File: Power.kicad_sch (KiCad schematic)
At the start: 97 parts, among them Q1 FDMC510P, U1 ZXCT1009F, U2 LT1763, U3 TPS62110, U34 LT3097, U35 LT8582, U36 TPS82150

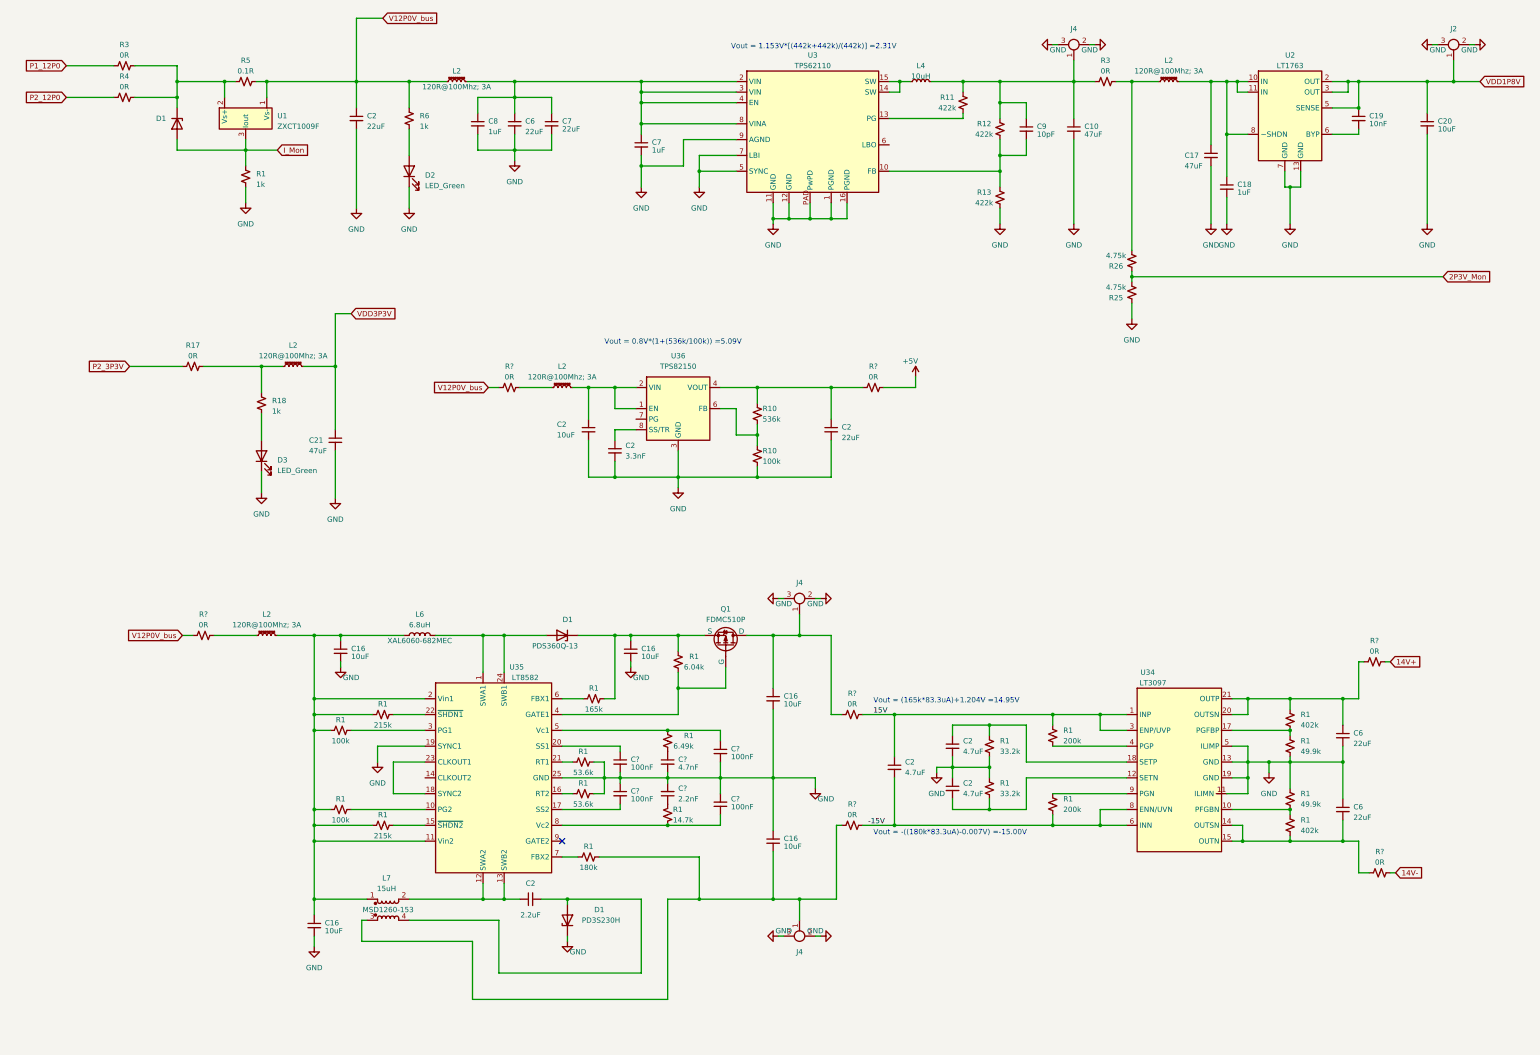
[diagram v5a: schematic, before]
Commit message: Updated Schematic
-Changed PPS input signal buffer
-Made Tweaks to Power Supply section  (Many involving the LT3097) as suggested by Trent.
- general schematic clean up for readability
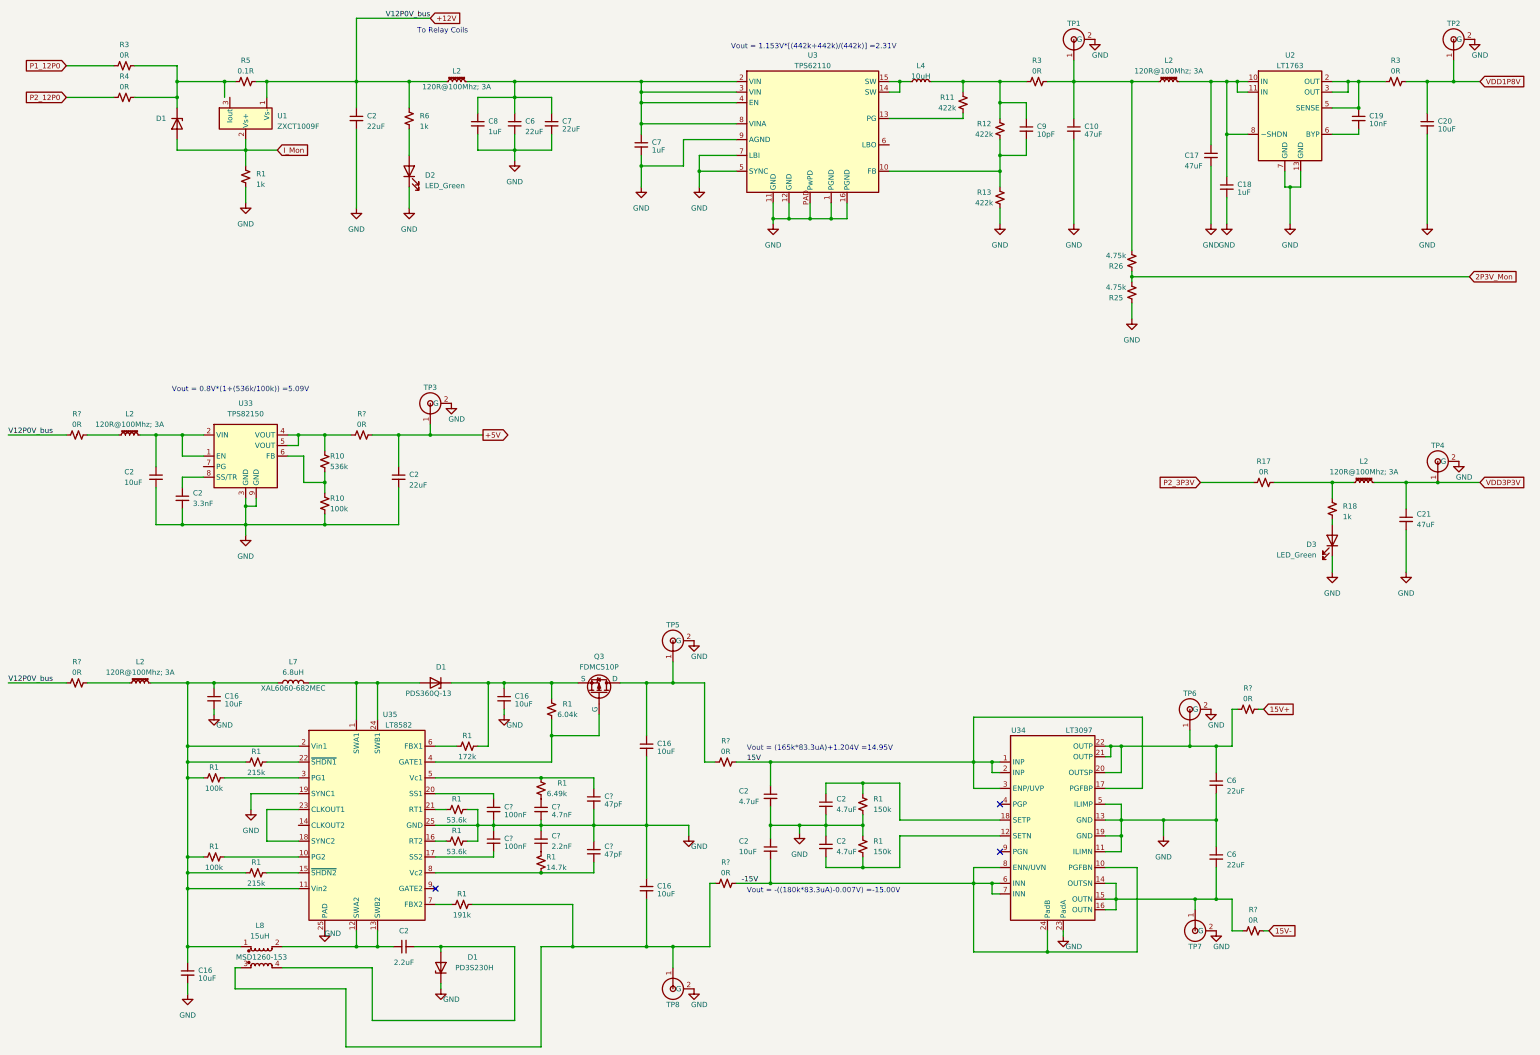
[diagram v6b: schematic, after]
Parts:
- removed J2, J4 (x3): ~, symbol Custom_Lib_MPEX_Zest:CONN_U-FL_SMD
- removed R1 (x2): 49.9k, symbol Device:R_Small_US
- removed R1: 33.2k, symbol Device:R_Small_US
- removed R1 (x2): 200k, symbol Device:R_Small_US
- removed R1 (x2): 402k, symbol Device:R_Small_US
- removed R3: 0R, symbol Device:R_Small_US
- removed R?: 0R, Capacitor_SMD:C_0603_1608Metric, symbol Device:R_Small_US
- added C2: 10uF, symbol Device:C_Small
- added R1: 150k, Resistor_SMD:R_0603_1608Metric, symbol Device:R_Small_US
- added R3 (x2): 0R, symbol Device:R_Small_US
- added R?: 0R, Capacitor_SMD:C_0603_1608Metric, symbol Device:R_Small_US
- added TP1, TP2, TP3, TP4, TP5, TP6, TP7, TP8: ~, symbol AD7768_Digitizer_SLib:Test_Point_MMCC
- C? (x2): value 100nF -> 47pF; MPN CL10B104KB8NNWC -> (none)
- R1: value 33.2k -> 150k; footprint (none) -> Resistor_SMD:R_0603_1608Metric
- R1: value 165k -> 172k
- R1: value 180k -> 191k
- renumbered L6 to L7, L7 to L8, Q1 to Q3, U36 to U33
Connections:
- net +5V: now also C2.1, R?.2, TP3.1
- net -15V: now also U34.10 (PGFBN), U34.24 (PadB), U34.7 (INN), C2.2; no longer C2.2
- net 15V: now also U34.17 (PGFBP), U34.2 (INP)
- net GND: now also C2.2, U34.23 (PadA), C2.1, R1.1, TP1.2 (G), TP2.2 (G), TP3.2 (G), TP4.2 (G), TP5.2 (G), TP6.2 (G), TP7.2 (G), TP8.2 (G)
- net I_Mon: now also U1.2 (Vs+); no longer U1.3 (Iout)
- net VDD1P8V: now also R3.2, TP2.1; no longer C19.1, U2.2 (OUT), U2.3 (OUT), U2.5 (SENSE)
- net VDD3P3V: now also TP4.1
- net at C2.2, U34.12 (SETN): now also R1.2
- net at C16.1, Q3.1 (D), R?.1: now also TP5.1
- net at C6.2, R?.1, U34.14 (OUTSN)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: now also U34.16 (OUTN), TP7.1
- net at C6.1, R?.1, U34.20 (OUTSP)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: now also U34.22 (OUTP), TP6.1
- net at C16.2, L8.3, R1.2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: now also TP8.1
- net at C9.1, L4.2, R11.1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: now also R3.1; no longer C10.1
- net at L2.1, R26.2: now also C10.1, R3.2, TP1.1
- net at R10.1, U33.4 (VOUT), U33.5 (VOUT): now also R?.1; no longer C2.1
- net at D1.1 (K), R3.2, R4.2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: no longer U1.2 (Vs+)
- net 14V+ renamed 15V+
- net 14V- renamed 15V-
- net V12P0V_bus renamed +12V
- new net: C19.1, R3.1, U2.2 (OUT), U2.3 (OUT), U2.5 (SENSE)
- no-connect marks 1 -> 3
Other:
- note added: "To Relay Coils"
- moved on the sheet: C16, C2, C21, C6, C?, D1, D3, L2, L7, L8, Q3, R1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

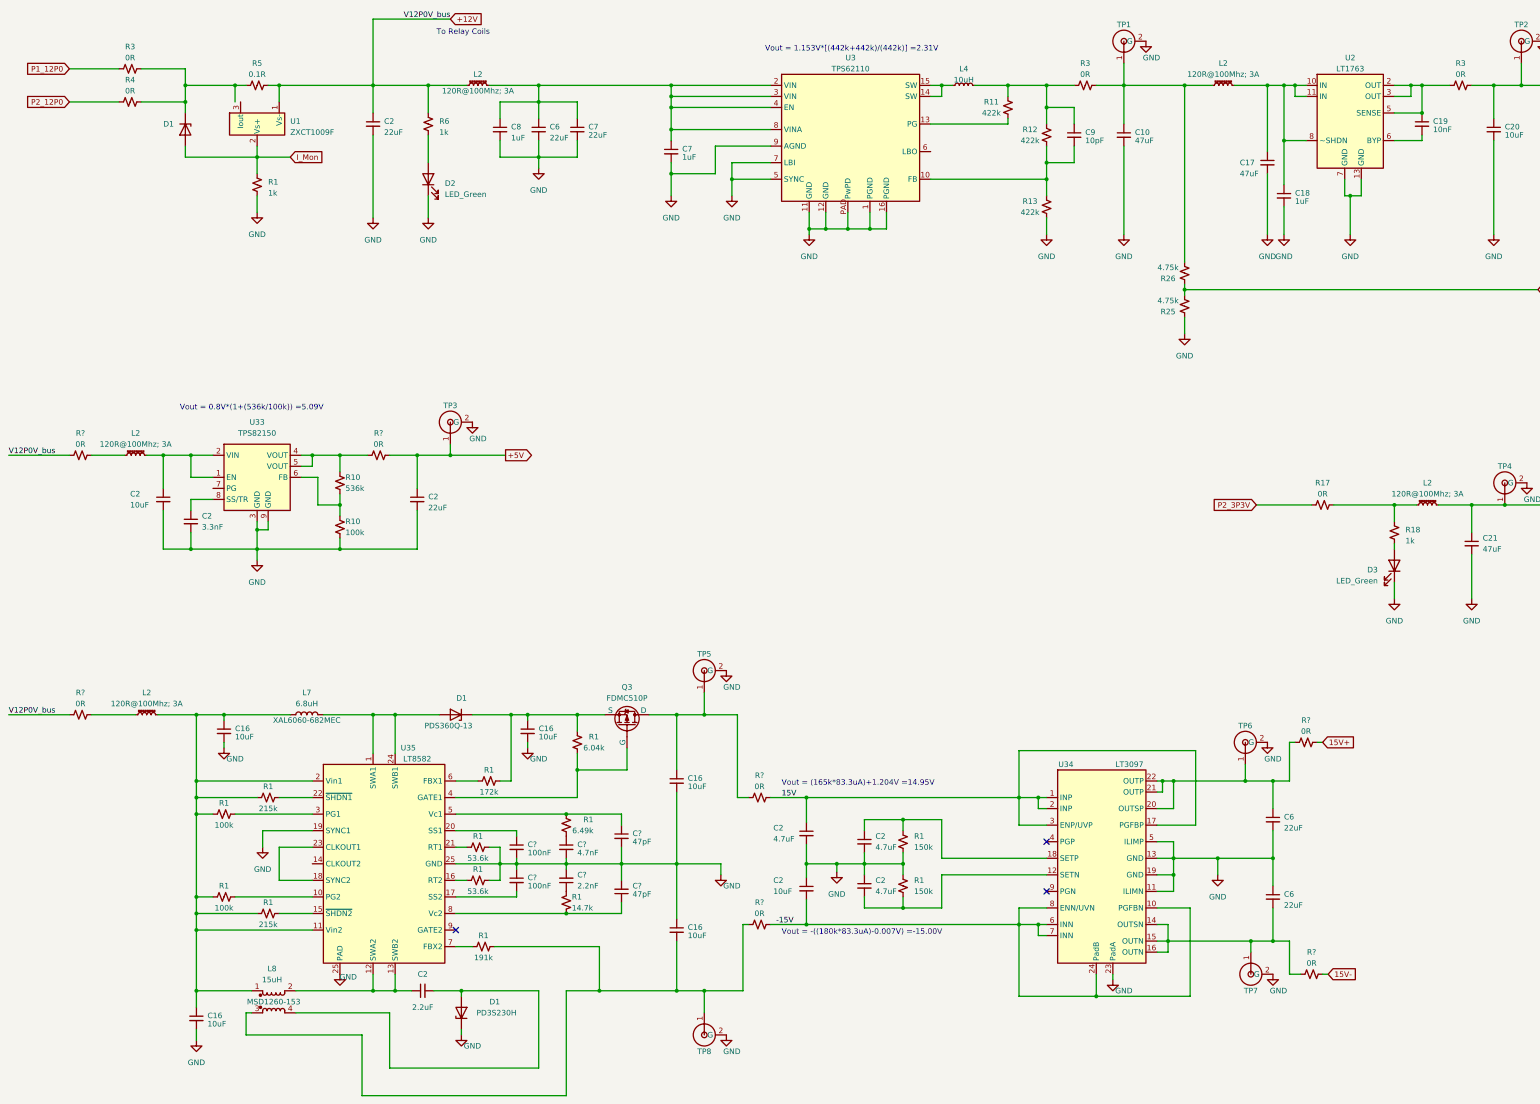
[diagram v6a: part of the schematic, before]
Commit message: Update to Schematics; initial PCB commit
-Updated Power, Housekeeping, and ADCs sheets.
-Remapped FMC pins
-Initial board layout commit
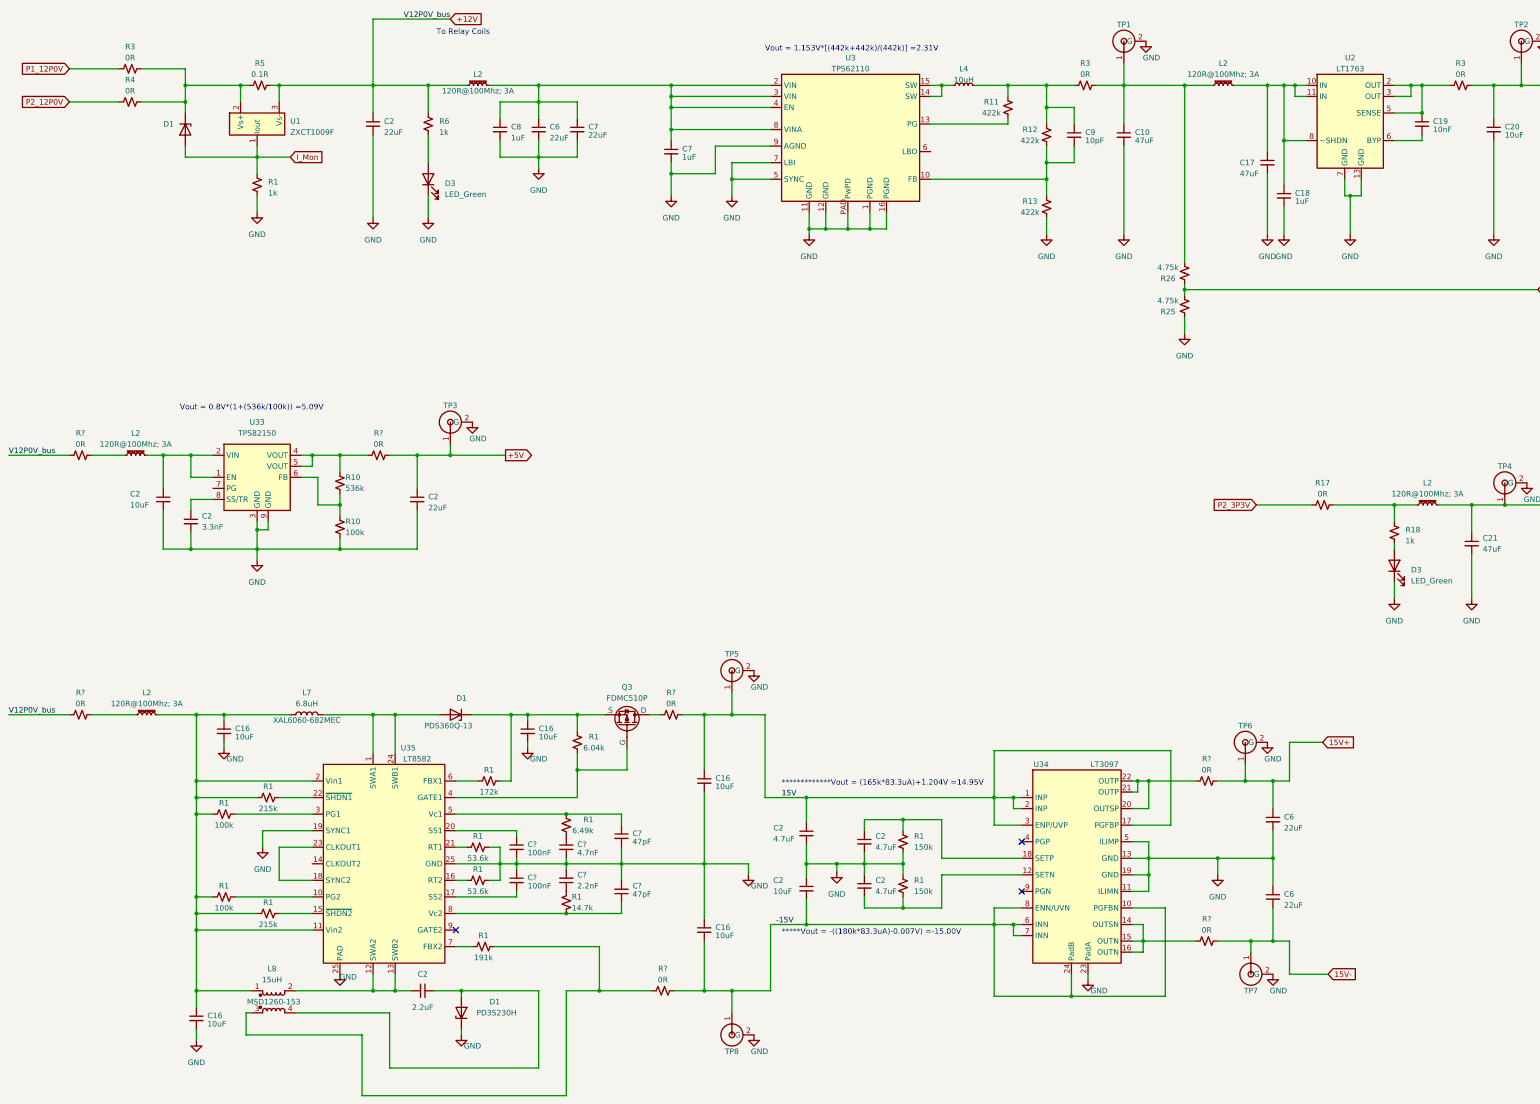
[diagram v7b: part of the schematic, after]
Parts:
- removed D2, D3: LED_Green, symbol Device:LED
- removed R? (x4): 0R, Capacitor_SMD:C_0603_1608Metric, symbol Device:R_Small_US
- added D3 (x2): LED_Green, LED_SMD:LED_0603_1608Metric, symbol Device:LED
- added R? (x4): 0R, Resistor_SMD:R_0603_1608Metric, symbol Device:R_Small_US
- C10, C16, C17, C2, C20, C21, C6, C7: footprint (none) -> Capacitor_SMD:C_0805_2012Metric
- C18, C19, C2, C7, C8, C9: footprint (none) -> Capacitor_SMD:C_0603_1608Metric
- L2: footprint (none) -> Inductor_SMD:L_0805_2012Metric
- L4, L7: footprint (none) -> footprints:IND_7345-WE-PD_WRE
- L8: footprint (none) -> footprints:MSD1260153MLD
- R1, R10, R11, R12, R13, R17, R18, R25, R26, R3, R6: footprint (none) -> Resistor_SMD:R_0603_1608Metric
- R1, R3, R4, R5: footprint (none) -> Resistor_SMD:R_0805_2012Metric
- R? (x3): footprint Capacitor_SMD:C_0603_1608Metric -> Resistor_SMD:R_0603_1608Metric
- TP1, TP2, TP3, TP4, TP5, TP6, TP7, TP8: footprint (none) -> TestPoint:TestPoint_Loop_D1.80mm_Drill1.0mm_Beaded
- U2: footprint (none) -> Package_DFN_QFN:DFN-12-1EP_3x4mm_P0.5mm_EP1.7x3.3mm
- U3: footprint (none) -> Package_DFN_QFN:QFN-16-1EP_4x4mm_P0.65mm_EP2.7x2.7mm_PullBack
- U33: footprint Package_LGA:Texas_MicroSiP-8-1EP_2.8x3.0mm_P0.65mm_EP1.1x1.9mm_SMD_ThermalVias -> footprints:SIL0008D_SMD
- U34: footprint (none) -> footprints:05-08-7071_ADI-M
- U35: footprint (none) -> Package_DFN_QFN:DFN-24-1EP_4x7mm_P0.5mm_EP2.64x6.44mm
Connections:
- net +12V: now also U1.3 (Vs-); no longer U1.1 (Vs-)
- net -15V: now also C16.2, TP8.1, R?.2
- net 15V: now also C16.1, TP5.1, R?.2
- net 15V+: now also C6.1, TP6.1, R?.2
- net 15V-: now also C6.2, TP7.1, R?.2
- net GND: now also D3.1 (K), D3.1 (K)
- net I_Mon: now also U1.1 (Iout); no longer U1.2 (Vs+)
- net at U34.14 (OUTSN), U34.15 (OUTN), U34.16 (OUTN): now also R?.1; no longer C6.2, TP7.1
- net at U34.20 (OUTSP), U34.21 (OUTP), U34.22 (OUTP): now also R?.1; no longer C6.1, TP6.1
- net at L8.3, R1.2: now also R?.1; no longer C16.2, TP8.1
- net at R6.1: now also D3.2 (A)
- net at R18.1: now also D3.2 (A)
- net at D1.1 (K), R3.2, R4.2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: now also U1.2 (Vs+)
- net P1_12P0 renamed P1_12P0V
- net P2_12P0 renamed P2_12P0V
- new net: Q3.1 (D), R?.1
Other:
- note added: "*************Vout = (165k*83.3uA)+1.204V =14.95V"
- note added: "*****Vout = -((180k*83.3uA)-0.007V) =-15.00V"
- note removed: "Vout = (165k*83.3uA)+1.204V =14.95V"
- note removed: "Vout = -((180k*83.3uA)-0.007V) =-15.00V"
- moved on the sheet: C16, R5, TP5, TP8, U34

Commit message: Updated Layout
-Additional Layout Work
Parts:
- added TP10, TP9: ~, TestPoint:TestPoint_Loop_D1.80mm_Drill1.0mm_Beaded, symbol Connector:TestPoint
- C? (x2): footprint Capacitor_SMD:C_0603_1608Metric -> Capacitor_SMD:C_0402_1005Metric
- D1: footprint (none) -> Diode_SMD:D_SOD-323_HandSoldering
- D1: value ~ -> BAT54W; footprint (none) -> Package_TO_SOT_SMD:SOT-323_SC-70; MPN (none) -> BAT54W-7-F
- D1: footprint (none) -> Diode_SMD:D_PowerDI-5
- Q3: footprint (none) -> footprints:MLP8_3P3X3P3_ONS-M; MPN (none) -> FDMC510P
- R1: footprint Resistor_SMD:R_0603_1608Metric -> Resistor_SMD:R_0402_1005Metric
- R5: footprint Resistor_SMD:R_0805_2012Metric -> Resistor_SMD:R_1206_3216Metric; MPN (none) -> ERJ-8BWFR100V
- R6: value 1k -> 5.6k
- TP1, TP2, TP3, TP4, TP5, TP6, TP7, TP8: symbol AD7768_Digitizer_SLib:Test_Point_MMCC -> Connector:TestPoint
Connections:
- net GND: now also U3.17 (PwPD), TP10.1, TP9.1; no longer TP1.2 (G), TP2.2 (G), TP3.2 (G), TP4.2 (G), TP5.2 (G), TP6.2 (G), TP7.2 (G), TP8.2 (G), U3.PAD (PwPD)
- net LT3097_VOUT-: now reaches R?.1, U34.14 (OUTSN), U34.15 (OUTN), U34.16 (OUTN)
- net LT3097_VOUT+: now reaches R?.1, U34.20 (OUTSP), U34.21 (OUTP), U34.22 (OUTP)
- net TPS62110_VIN: now reaches C6.1, C7.1, C7.1, C8.1, L2.2, U3.2 (VIN), U3.3 (VIN), U3.4 (EN), U3.8 (VINA)
- net LT8582_VIN: now reaches C16.1, C16.1, L2.2, L7.1, L8.1, R1.1, R1.1, R1.1, R1.1, U35.11 (Vin2)
- net LT8582_VIN: no longer U35.2 (Vin1)
- net TPS82150_VOUT: now reaches R10.1, R?.1, U33.4 (VOUT), U33.5 (VOUT)
- net -15V renamed -16V
- net 15V renamed 16V
- no-connect marks 3 -> 5
